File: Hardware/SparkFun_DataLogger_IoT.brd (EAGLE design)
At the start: 50.8 x 38.1 mm, 139 parts, among them J10 QWIIC_RIGHT_ANGLE, J3 MICRO-SD-PUSH-PUSH-EXT-PIN, J4 Vertical Qwiic Connector, U1 ESP-WROOM-32E, U10 74HC4066_QUAD_BILATERAL_SWITC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, U2 CH340C, U3 XC6222B331MR-G, U4 MAX17048, U5 MCP73831, U6 XC6222B331MR-G, U9 74HC4066_QUAD_BILATERAL_SWITC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

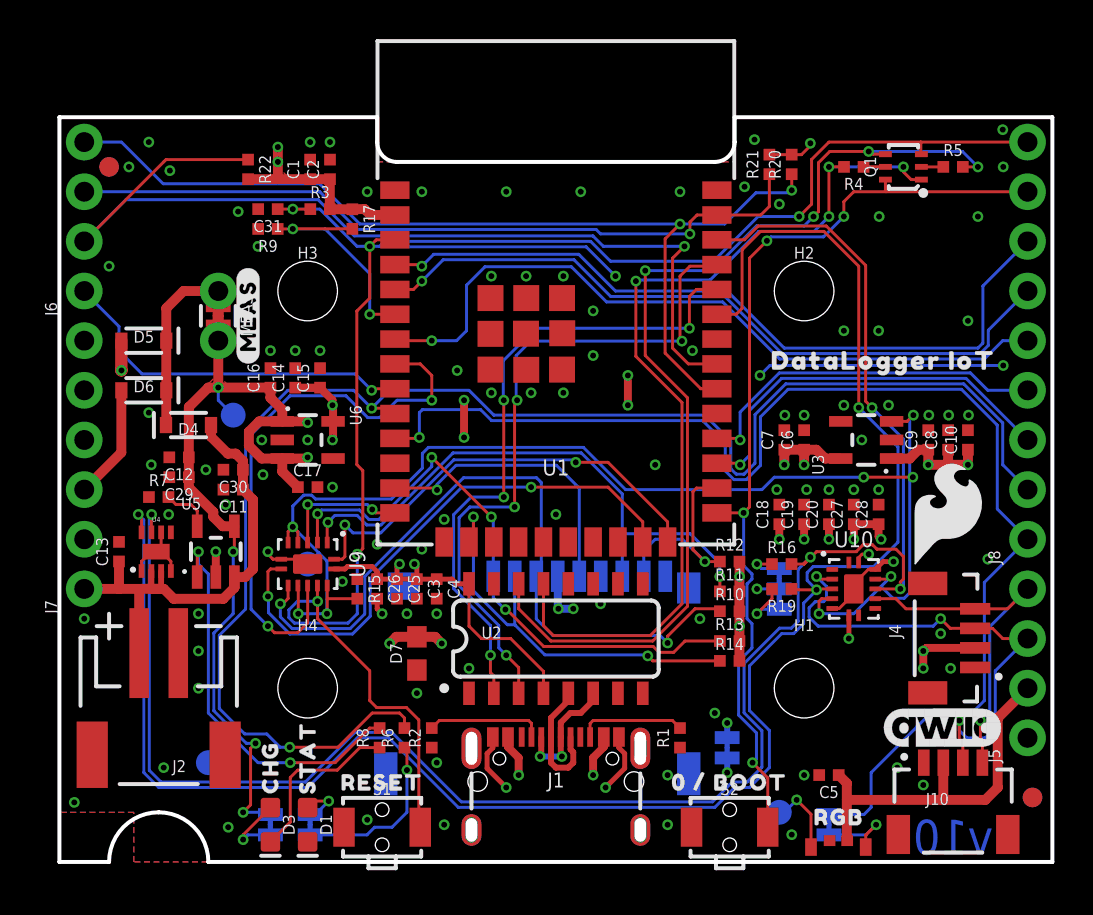
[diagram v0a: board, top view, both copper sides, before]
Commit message: Pre-Design Review updates
Add 9.1k Res for hardware versioning.
Move MEAS to be on grid.
Shuffle diodes around a little.
Move silk to fill gaps.
Change LED bias resistor to meet standards.
Made HW versioning be on A7 to match RTK designs.
Replaced A7 breakout with D5.
Relabeled silk.
Added silk to RGB LED.
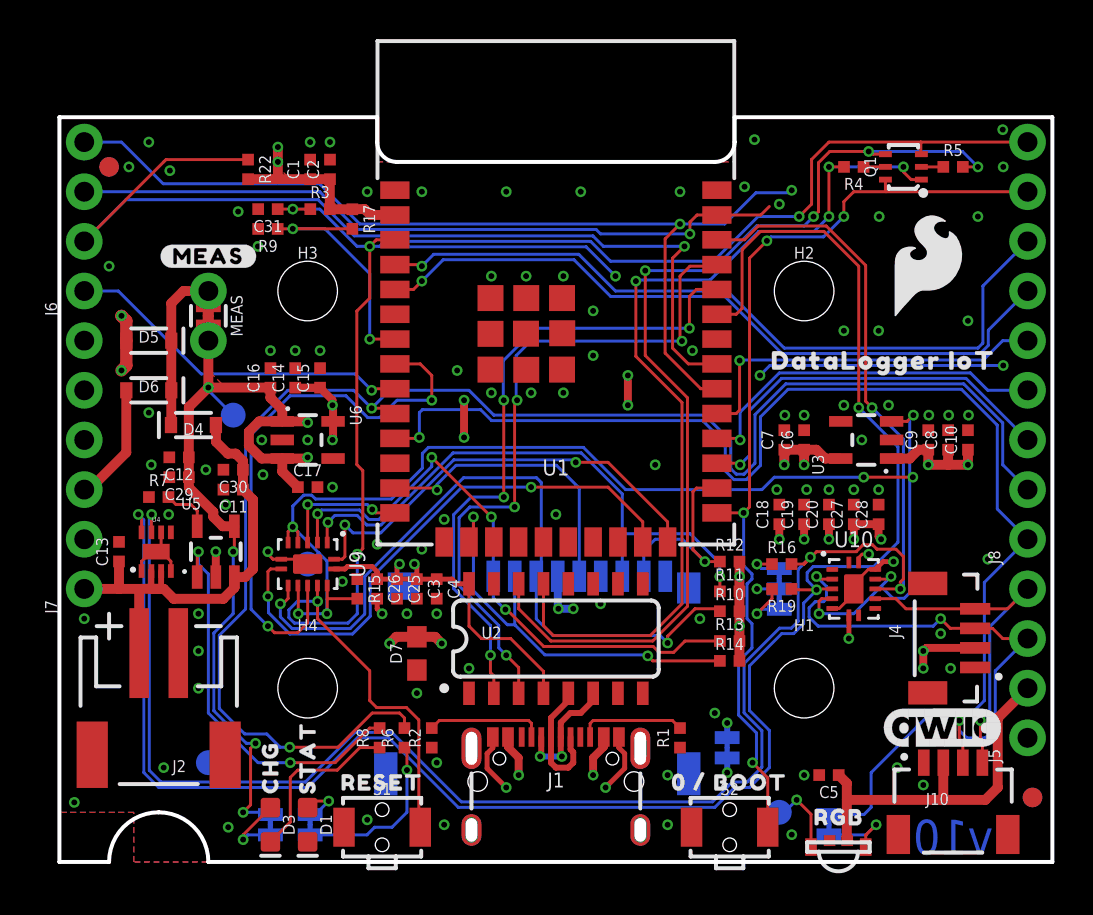
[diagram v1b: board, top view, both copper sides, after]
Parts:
- removed R20, R21: 100k, SparkFun-Resistors:0402-TIGHT
- removed U$20: (no value), output:#35_#_A7#0
- added U$12: (no value), output:#5_#_D5#0
- R17: value 1M -> 100k
- R6: value 1k -> 2.2k
- R9: value 93.1k -> 9.1K; device SparkFun-Resistors:0402-TIGHT -> RA_RGB:0402-TIGHT
- moved LOGO6 12.7 mm to (44.5, 30.5)
- moved U$9 3.66 mm to (7.62, 31.0), turned to 0 degrees
- moved MEAS 0.51 mm to (7.62, 27.9)
- moved U$10 0.51 mm to (9.14, 27.9)
- moved D5 0.25 mm to (4.57, 26.7)
- moved D6 0.25 mm to (4.57, 24.1)
- moved D4 0.25 mm to (6.86, 22.4)
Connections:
- removed net ESP34/A6: R17.2, R9.1, U1.6
- new net ESP5: J8.5, U1.29
- net 3.3V: no longer R20.2, R21.2
- net ESP18/SCK: no longer R20.1
- net ESP23/PICO: no longer R21.1
- net ESP35/A7: now also R17.2, R9.1; no longer J8.5
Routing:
- net ESP35/A7: track 37.7 -> 13.3 mm, vias 1 -> 2
- net ESP5: track 0.00 -> 18.9 mm, vias 0 -> 1
- net ESP34/A6: track 12.1 -> 0.00 mm, vias 2 -> 0
- net V_USB: track 52.8 -> 57.0 mm, vias 5 -> 6
- net 3.3V: track 43.0 -> 40.6 mm, vias 15 -> 14
- net ESP23/PICO: track 38.5 -> 36.9 mm
- net ESP18/SCK: track 49.8 -> 49.0 mm
- net ESP33: track 18.8 -> 18.0 mm
- net N$3: track 9.77 -> 9.16 mm
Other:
- board text added: "4-Layers 1.6mm Thickness 1oz Copper Lead-Free HASL Finish Red Solder Resist White Silkscreen Controlled Impedance: JLC7628 Material: TG155"
- board text removed: "4-Layers 1.6mm Thickness 1oz Copper Lead-Free HASL Finish Red Solder Resist White Silkscreen"

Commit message: Post design review updates.
Change BO silk for D5.
Remove unused PURs.
Clean up wire stubs.
Remove GND guard trace.
Add GND vias near switching vias.
Renumber Schematic.
Repanelize and pull together outer border.
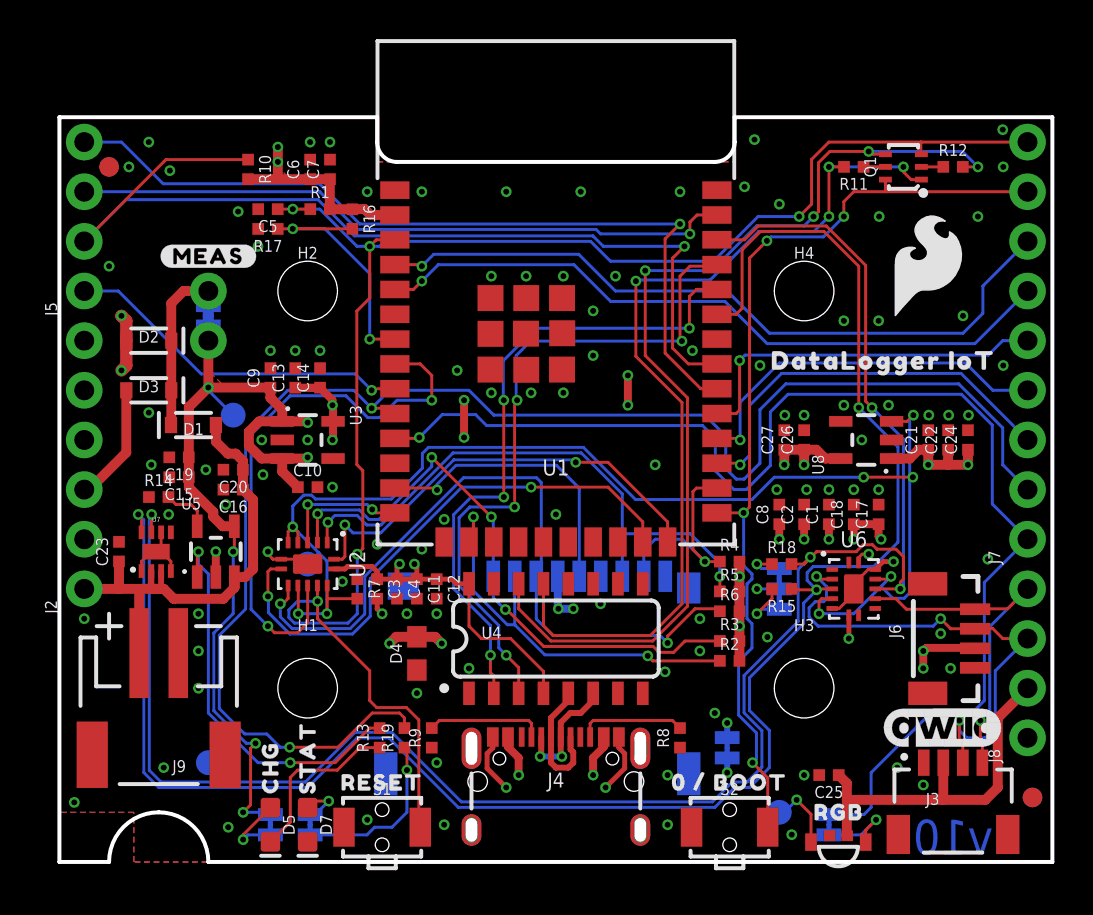
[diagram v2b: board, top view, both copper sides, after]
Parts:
- removed C28, C29, C30: 2.2uF, SparkFun-Capacitors:0402-TIGHT
- removed C31: 0.1uF, SparkFun-Capacitors:0402-TIGHT
- removed J10: QWIIC_RIGHT_ANGLE, SparkFun-Connectors:JST04_1MM_RA
- removed R22: 10k, SparkFun-Resistors:0402-TIGHT
- removed U10, U9: 74HC4066_QUAD_BILATERAL_SWITCH_QFN, SparkFun-IC-Logic:14-QFN
- added C21, C22, C24: 2.2uF, SparkFun-Capacitors:0402-TIGHT
- added C23: 0.1uF, SparkFun-Capacitors:0402-TIGHT
- added J9: (no value), SparkFun-Connectors:JST-2-SMD
- added R18: 2.2k, SparkFun-Resistors:0402-TIGHT
- added U7: MAX17048, SparkFun-IC-Power:DFN-8
- added U8: XC6222B331MR-G, SparkFun-IC-Power:SOT23-5
- C10, C14, C27, C5: value 2.2uF -> 0.1uF
- C12: value 2.2uF -> 10nF
- C13, C15, C17, C19: value 0.1uF -> 2.2uF
- C4: value 10nF -> 2.2uF
- D1: value BLUE -> 3A/10V/280mV; device SparkFun-LED:LED-0603 -> SparkFun-DiscreteSemi:SOD-323
- D2: value B3DQ3BRG -> 3A/10V/280mV; device RA_RGB:B3DQ3BRG -> SparkFun-DiscreteSemi:SOD-323
- D3: value Yellow -> 3A/10V/280mV; device SparkFun-LED:LED-0603 -> SparkFun-DiscreteSemi:SOD-323
- D4: value 3A/10V/280mV -> TVS; device SparkFun-DiscreteSemi:SOD-323 -> SparkFun-DiscreteSemi:0603
- D5: value 3A/10V/280mV -> Yellow; device SparkFun-DiscreteSemi:SOD-323 -> SparkFun-LED:LED-0603
- D6: value 3A/10V/280mV -> B3DQ3BRG; device SparkFun-DiscreteSemi:SOD-323 -> RA_RGB:B3DQ3BRG
- D7: value TVS -> BLUE; device SparkFun-DiscreteSemi:0603 -> SparkFun-LED:LED-0603
- J1: value (none) -> MICRO-SD-PUSH-PUSH-EXT-PIN; device SparkFun-Connectors:USB-C-16P_4LAYER-PADS -> SparkFun-Connectors:MICROSD-EXTERNALPIN
- J2: device SparkFun-Connectors:JST-2-SMD -> SparkFun-Connectors:1X06_NO_SILK
- J3: value MICRO-SD-PUSH-PUSH-EXT-PIN -> QWIIC_RIGHT_ANGLE; device SparkFun-Connectors:MICROSD-EXTERNALPIN -> SparkFun-Connectors:JST04_1MM_RA
- J4: value Vertical Qwiic Connector -> (none); device SparkFun-Connectors:JST04_1MM_VERT -> SparkFun-Connectors:USB-C-16P_4LAYER-PADS
- J6: value (none) -> Vertical Qwiic Connector; device SparkFun-Connectors:1X04_NO_SILK -> SparkFun-Connectors:JST04_1MM_VERT
- J7: device SparkFun-Connectors:1X06_NO_SILK -> SparkFun-Connectors:1X09_NO_SILK
- J8: device SparkFun-Connectors:1X09_NO_SILK -> SparkFun-Connectors:1X04_NO_SILK
- LOGO1: value SPECIAL_INSTRUCTIONS-ORDERING -> SFE_LOGO_NAME.2_INCH; device SparkFun-Aesthetics:ORDERING_INSTRUCTIONS -> SparkFun-Aesthetics:SFE_LOGO_NAME_.2
- LOGO3: value QWIIC_LOGO_6MM -> SPECIAL_INSTRUCTIONS-ORDERING; device SparkFun-Aesthetics:QWIIC_6MM -> SparkFun-Aesthetics:ORDERING_INSTRUCTIONS
- LOGO4: value OSHW-LOGOS -> QWIIC_LOGO_6MM; device SparkFun-Aesthetics:OSHW-LOGO-S -> SparkFun-Aesthetics:QWIIC_6MM
- LOGO5: value SFE_LOGO_NAME.2_INCH -> OSHW-LOGOS; device SparkFun-Aesthetics:SFE_LOGO_NAME_.2 -> SparkFun-Aesthetics:OSHW-LOGO-S
- R1, R2: value 5.1k -> 10k
- R13: value 10k -> 1k
- R14: value 10k -> 2.0K
- R15: value 10k -> 2.2k
- R16: value 2.2k -> 100k
- R17: value 100k -> 9.1K; device SparkFun-Resistors:0402-TIGHT -> RA_RGB:0402-TIGHT
- R6: value 2.2k -> 10k
- R7: value 2.0K -> 10k
- R8: value 1k -> 5.1k
- R9: value 9.1K -> 5.1k; device RA_RGB:0402-TIGHT -> SparkFun-Resistors:0402-TIGHT
- U$12: device output:#5_#_D5#0 -> output:#5#0
- U2: value CH340C -> 74HC4066_QUAD_BILATERAL_SWITCH_QFN; device SparkFun-IC-Comms:SO016 -> SparkFun-IC-Logic:14-QFN
- U4: value MAX17048 -> CH340C; device SparkFun-IC-Power:DFN-8 -> SparkFun-IC-Comms:SO016
- U6: value XC6222B331MR-G -> 74HC4066_QUAD_BILATERAL_SWITCH_QFN; device SparkFun-IC-Power:SOT23-5 -> SparkFun-IC-Logic:14-QFN
- moved FD1 57.2 mm to (49.8, 3.30), flipped to the top
- moved FD2 57.2 mm to (49.8, 3.30), flipped to the bottom
- moved FD3 57.2 mm to (2.54, 35.6)
- moved FD4 57.2 mm to (2.54, 35.6)
- moved J5 53.4 mm to (1.27, 29.2)
- moved LOGO3 50.7 mm to (62.2, 54.6)
- moved J6 49.6 mm to (47.6, 11.4)
- moved J7 48.3 mm to (49.5, 16.5)
- moved D2 43.8 mm to (4.57, 26.7), turned to 180 degrees
- moved LOGO1 43.3 mm to (25.4, 31.8), flipped to the bottom
- moved D6 42.2 mm to (39.9, 1.02), turned to 270 degrees
- moved C5 40.8 mm to (10.7, 33.4)
- moved C10 33.9 mm to (12.7, 19.2), turned to 0 degrees
- moved C9 33.8 mm to (10.8, 24.8)
- moved R10 33.4 mm to (9.65, 35.4), turned to 270 degrees
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- renumbered LOGO6 to LOGO2, PWREN to TP4, VIN to TP2, VIN1 to TP3
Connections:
- net !RESET!: now also C5.1, J7.9, R1.1, U2.12; no longer C31.1, J8.9, R3.1, U9.12
- net 3.3V: now also C11.1, C12.1, C13.1, C17.1, C18.1, C6.1, C7.1, J2.5, R1.2, R10.2, R16.1, U2.14, U3.5, U4.16, U4.4, U6.14; no longer C1.1, C15.1, C2.1, C25.1, C26.1, C27.1, C28.1, J7.5, R17.1, R22.2, R3.2, U10.14, U2.16, U2.4, U6.5, U9.14
- net 3.3V_SW: now also C1.1, C2.1, C25.1, C26.1, C27.1, C8.1, D6.2, J1.4, J3.2, J6.2, J8.2, R2.2, R3.2, R4.2, R5.2, R6.2, U8.5; no longer C18.1, C19.1, C20.1, C5.1, C6.1, C7.1, D2.2, J10.2, J3.4, J4.2, J5.2, R10.2, R11.2, R12.2, R13.2, R14.2, U3.5
- net 5V: now also D3.A, J2.3; no longer D6.A, J7.3
- net CH340-DTR: now also R11.2, U4.13; no longer R4.2, U2.13
- net CH340-RTS: now also R12.2, U4.14; no longer R5.2, U2.14
- net CH340-RX: now also U4.3; no longer U2.3
- net CH340-TX: now also U4.2; no longer U2.2
- net D+: now also J4.A6, J4.B6, U4.5; no longer J1.A6, J1.B6, U2.5
- net D-: now also J4.A7, J4.B7, U4.6; no longer J1.A7, J1.B7, U2.6
- net ESP0/!BOOT!: now also J7.8; no longer J8.8
- net ESP12/DAT2: now also U2.4; no longer U9.4
- net ESP13/DAT3: now also J1.2, R2.1; no longer J3.2, R14.1
- net ESP14/CLK: now also J1.5; no longer J3.5
- net ESP15/CMD: now also U2.8; no longer U9.8
- net ESP16/RXD: now also J7.3; no longer J8.3
- net ESP17/TXD: now also J7.4; no longer J8.4
- net ESP18/SCK: now also J5.4; no longer J6.4
- net ESP19/POCI: now also J5.2, R10.1; no longer J6.2, R22.1
- net ESP2/DAT0: now also U2.1; no longer U9.1
- net ESP21/SDA: now also R15.1, U6.4, U7.8; no longer R19.1, U10.4, U4.8
- net ESP22/SCL: now also R18.2, U6.11, U7.7; no longer R16.2, U10.11, U4.7
- net ESP23/PICO: now also J5.3; no longer J6.3
- net ESP25/LED: now also J7.2, R19.2; no longer J8.2, R6.2
- net ESP26/RGBLED: now also J7.1; no longer J8.1
- net ESP32/PWREN: now also U2.11; no longer U9.11
- net ESP33: now also J5.1; no longer J6.1
- net ESP35/A7: now also R16.2, R17.1; no longer R17.2, R9.1
- net ESP36/A0: now also J7.7; no longer J8.7
- net ESP39/A3: now also J7.6; no longer J8.6
- net ESP4/DAT1: now also J1.8, R4.1; no longer J3.8, R12.1
- net ESP5: now also J7.5; no longer J8.5
- net GND: now also C21.2, C22.2, C23.2, C24.2, D4.1, D6.1, D7.C, J1.10, J1.11, J1.12, J1.13, J1.6, J2.2, J2.4, J2.6, J3.1, J4.GND, J4.GND2, J6.1, J8.1, J9.1, R14.1, R17.2, R8.1, R9.1, U2.7, U2.EPAD, U6.13, U6.6, U6.7, U6.EPAD, U7.1, U7.4, U7.6, U7.9, U8.2; no longer C28.2, C29.2, C30.2, C31.2, D1.C, D2.1, D7.1, J1.GND, J1.GND2, J10.1, J2.1, J3.10, J3.11, J3.12, J3.13, J3.6, J4.1, J5.1, J7.2, J7.4, J7.6, R1.1, R15.1, R2.1, R9.2, U10.13, U10.6, U10.7, U10.EPAD, U2.1, U4.4, U4.6, U4.9, U6.2, U9.7, U9.EPAD
- net N$1: now also J4.B5, R8.2; no longer J1.B5, R1.2
- net N$10: now also R13.2; no longer R8.2
- net N$11: now also R14.2; no longer R7.2
- net N$12: now also D6.3; no longer D2.3
- net N$13: now also D7.A; no longer D1.A
- net N$16: now also R18.1; no longer R16.1
- net N$17: now also R15.2; no longer R19.2
- net N$2: now also J4.A5, R9.2; no longer J1.A5, R2.2
- net N$3: now also D1.C, D2.C, D3.C; no longer D4.C, D5.C, D6.C
- net N$4: now also R12.1; no longer R5.1
- net N$5: now also R11.1; no longer R4.1
- net N$6: now also R19.1; no longer R6.1
- net N$7: now also D6.4; no longer D2.4
- net N$8: now also D5.A; no longer D3.A
- net N$9: now also D5.C, R13.1; no longer D3.C, R8.1
- net PWREN: now also R7.2, U2.10, U2.13, U2.5, U2.6, U6.12, U6.5, U8.3; no longer R15.2, U10.12, U10.5, U3.3, U9.10, U9.13, U9.5, U9.6
- net QWIIC_SCL: now also J3.4, J6.4, J8.4, U6.10; no longer J10.4, J4.4, J5.4, U10.10
- net QWIIC_SDA: now also J3.3, J6.3, J8.3, U6.3; no longer J10.3, J4.3, J5.3, U10.3
- net SD_CMD: now also J1.3, R6.1, U2.9; no longer J3.3, R10.1, U9.9
- net SD_DAT0: now also J1.7, R5.1, U2.2; no longer J3.7, R11.1, U9.2
- net SD_DAT2: now also J1.1, R3.1, U2.3; no longer J3.1, R13.1, U9.3
- net SHIELD: now also J4.SHLD1, J4.SHLD2, J4.SHLD3, J4.SHLD4; no longer J1.SHLD1, J1.SHLD2, J1.SHLD3, J1.SHLD4
- net VIN: now also C15.1, C19.1, C21.1, C22.1, C24.1, U3.3, U8.1; no longer C12.1, C16.1, C17.1, C29.1, C8.1, U6.1, U6.3
- net V_BATT: now also C16.1, C20.1, C23.1, D1.A, J2.1, J9.2, U7.2, U7.3; no longer C11.1, C13.1, C30.1, D4.A, J2.2, J7.1, U4.2, U4.3
- net V_USB: now also D2.A, D4.2, J4.VBUS1, J4.VBUS2; no longer D5.A, D7.2, J1.VBUS1, J1.VBUS2
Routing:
- net GND: track 45.3 -> 21.1 mm, vias 101 -> 104
- net ESP18/SCK: track 49.0 -> 42.5 mm, vias 2 -> 1
- net ESP23/PICO: track 36.9 -> 34.0 mm
- net ESP36/A0: track 38.6 -> 37.1 mm
- net ESP39/A3: track 36.8 -> 35.7 mm
- net ESP17/TXD: track 18.5 -> 19.3 mm
- net ESP26/RGBLED: track 65.7 -> 65.1 mm
- added copper zone on layer 15, net 3.3V_SW

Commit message: Update for v11 PCB
Removed OSHW logo.
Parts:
- removed LOGO5: OSHW-LOGOS, SparkFun-Aesthetics:OSHW-LOGO-S
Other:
- board text added: "4-Layers 1.6mm Thickness 1oz Copper Lead-Free HASL Finish Red Solder Resist White Silkscreen Stackup: JLC7628 Material: TG155"
- board text added: "v11"
- board text removed: "4-Layers 1.6mm Thickness 1oz Copper Lead-Free HASL Finish Red Solder Resist White Silkscreen Controlled Impedance: JLC7628 Material: TG155"
- board text removed: "v10"
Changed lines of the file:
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@@
 Red Solder Resist
 White Silkscreen
-Controlled Impedance: JLC7628
+Stackup: JLC7628
 Material: TG155
 </text>
-<text x="45.72" y="0.381" size="1.778" layer="16" font="vector" ratio="15" rot="SMR0" align="bottom-center">v10</text>
+<text x="45.72" y="0.381" size="1.778" layer="16" font="vector" ratio="15" rot="SMR0" align="bottom-center">v11</text>
 <text x="-1.27" y="43.18" size="1.778" layer="47" font="vector" ratio="15" align="bottom-right">Dimensions
 In Inches</text>
@@
 <element name="FRAME1" library="SparkFun-Aesthetics" package="CREATIVE_COMMONS" value="FRAME-LEDGER" x="88.9" y="-5.08" smashed="yes">
 <attribute name="DESIGNER" value="Alex Brudner" x="168.91" y="-87.63" size="1.778" layer="27" display="off"/>
-<attribute name="REV" value="v10" x="168.91" y="-87.63" size="1.778" layer="27" display="off"/>
+<attribute name="REV" value="v11" x="168.91" y="-87.63" size="1.778" layer="27" display="off"/>
 </element>
 <element name="H3" library="SparkFun-Hardware" package="STAND-OFF-TIGHT" value="STAND-OFFTIGHT" x="38.1" y="8.89" smashed="yes">
@@
 <element name="U$37" library="output" package="#PICO_#_23#0" value="" x="2.032" y="34.29" smashed="yes" rot="MR0"/>
 <element name="U$38" library="output" package="#SCK_#_18#0" value="" x="2.032" y="36.83" smashed="yes" rot="MR0"/>
-<element name="LOGO5" library="SparkFun-Aesthetics" package="OSHW-LOGO-S" value="OSHW-LOGOS" x="25.4" y="17.78" smashed="yes" rot="MR0"/>
 <element name="U$45" library="output" package="#SHLD#0" value="" x="34.798" y="5.842" smashed="yes" rot="MR0"/>
 <element name="U$46" library="output" package="#I�C#0" value="" x="36.83" y="11.4935" smashed="yes" rot="MR0"/>

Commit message: NP unused resistors
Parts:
- R16: value 100k -> DNP; device SparkFun-Resistors:0402-TIGHT -> SparkFun-Resistors:0402-TIGHT_NO_CREAM
- R17: value 9.1K -> DNP; device RA_RGB:0402-TIGHT -> SparkFun-Resistors:0402-TIGHT_NO_CREAM
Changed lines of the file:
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@@
 <element name="LOGO1" library="SparkFun-Aesthetics" package="SFE_LOGO_NAME_.2" value="SFE_LOGO_NAME.2_INCH" x="25.4" y="31.75" smashed="yes" rot="MR0"/>
 <element name="LOGO2" library="SparkFun-Aesthetics" package="SFE_LOGO_FLAME_.2" value="SFE_LOGO_FLAME.2_INCH" x="44.45" y="30.48" smashed="yes"/>
-<element name="R17" library="RA_RGB" package="0402-TIGHT" value="9.1K" x="10.668" y="32.385" smashed="yes" rot="R180">
+<element name="R17" library="SparkFun-Resistors" package="0402-TIGHT_NO_CREAM" value="DNP" x="10.668" y="32.385" smashed="yes" rot="R180">
 <attribute name="NAME" x="10.668" y="31.823" size="0.6096" layer="25" font="vector" ratio="20" rot="R180" align="bottom-center"/>
-<attribute name="PN" value="RC0402FR-079K1L" x="10.668" y="32.385" size="1.778" layer="27" rot="R180" display="off"/>
-<attribute name="PROD_ID" value="RES-18504" x="10.668" y="32.385" size="1.778" layer="27" rot="R180" display="off"/>
-<attribute name="VALUE" value="9.1K" x="10.668" y="32.947" size="0.6096" layer="27" font="vector" ratio="20" rot="R180" align="top-center"/>
+<attribute name="VALUE" value="DNP" x="10.668" y="32.947" size="0.6096" layer="27" font="vector" ratio="20" rot="R180" align="top-center"/>
 </element>
-<element name="R16" library="SparkFun-Resistors" package="0402-TIGHT" value="100k" x="14.986" y="32.893" smashed="yes" rot="R270">
+<element name="R16" library="SparkFun-Resistors" package="0402-TIGHT_NO_CREAM" value="DNP" x="14.986" y="32.893" smashed="yes" rot="R270">
 <attribute name="NAME" x="15.548" y="32.893" size="0.6096" layer="25" font="vector" ratio="20" rot="R270" align="bottom-center"/>
-<attribute name="PROD_ID" value="RES-13495" x="14.986" y="32.893" size="1.778" layer="27" rot="R270" display="off"/>
-<attribute name="VALUE" value="100k" x="14.424" y="32.893" size="0.6096" layer="27" font="vector" ratio="20" rot="R270" align="top-center"/>
+<attribute name="VALUE" value="DNP" x="14.424" y="32.893" size="0.6096" layer="27" font="vector" ratio="20" rot="R270" align="top-center"/>
 </element>
 <element name="U$8" library="output" package="#_CHG#0" value="" x="10.795" y="4.826" smashed="yes" rot="MR90"/>

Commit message: Update VREG
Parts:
- U3, U8: value XC6222B331MR-G -> 3.3V
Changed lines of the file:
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@@
 <attribute name="VALUE" x="21.59" y="10.16" size="0.6096" layer="27"/>
 </element>
-<element name="U8" library="SparkFun-IC-Power" package="SOT23-5" value="XC6222B331MR-G" x="41.275" y="21.59" smashed="yes" rot="R90">
-<attribute name="IOUT" value="700mA" x="41.275" y="21.59" size="1.778" layer="27" rot="R90" display="off"/>
+<element name="U8" library="SparkFun-IC-Power" package="SOT23-5" value="3.3V" x="41.275" y="21.59" smashed="yes" rot="R90">
 <attribute name="NAME" x="39.116" y="19.812" size="0.6096" layer="25" ratio="20" rot="R90"/>
-<attribute name="PROD_ID" value="VREG-16775" x="135.255" y="83.82" size="1.778" layer="27" rot="R90" display="off"/>
-<attribute name="VOUT" value="3.3V" x="41.275" y="21.59" size="1.778" layer="27" rot="R90" display="off"/>
+<attribute name="PROD_ID" value="VREG-12457" x="135.255" y="83.82" size="1.778" layer="27" rot="R90" display="off"/>
+<attribute name="VALUE" value="3.3V" x="41.275" y="21.59" size="1.778" layer="27" rot="R90" display="off"/>
 </element>
 <element name="U7" library="SparkFun-IC-Power" package="DFN-8" value="MAX17048" x="4.953" y="15.875" smashed="yes">
@@
 <attribute name="VALUE" x="6.223" y="13.081" size="0.6096" layer="27" ratio="20"/>
 </element>
-<element name="U3" library="SparkFun-IC-Power" package="SOT23-5" value="XC6222B331MR-G" x="12.7" y="21.59" smashed="yes" rot="R270">
-<attribute name="IOUT" value="700mA" x="12.7" y="21.59" size="1.778" layer="27" rot="R270" display="off"/>
+<element name="U3" library="SparkFun-IC-Power" package="SOT23-5" value="3.3V" x="12.7" y="21.59" smashed="yes" rot="R270">
 <attribute name="NAME" x="14.859" y="23.368" size="0.6096" layer="25" ratio="20" rot="R270"/>
-<attribute name="PROD_ID" value="VREG-16775" x="-81.28" y="-44.45" size="1.778" layer="27" rot="R270" display="off"/>
-<attribute name="VOUT" value="3.3V" x="12.7" y="21.59" size="1.778" layer="27" rot="R270" display="off"/>
+<attribute name="PROD_ID" value="VREG-12457" x="-81.28" y="-44.45" size="1.778" layer="27" rot="R270" display="off"/>
+<attribute name="VALUE" value="3.3V" x="12.7" y="21.59" size="1.778" layer="27" rot="R270" display="off"/>
 </element>
 <element name="C4" library="SparkFun-Capacitors" package="0402-TIGHT" value="2.2uF" x="17.272" y="13.97" smashed="yes" rot="R270">
